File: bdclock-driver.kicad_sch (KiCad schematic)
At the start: 32 parts, among them J1 PWR, J2 Ctrl, J3 Anodes, J4 Kathodes, U1 NE555P, U2 74HC4017, U3 LM7805_TO220, U4 74HC595, U5 74HC595, U6 74HC595, U7 74LS138, U8 74LS138

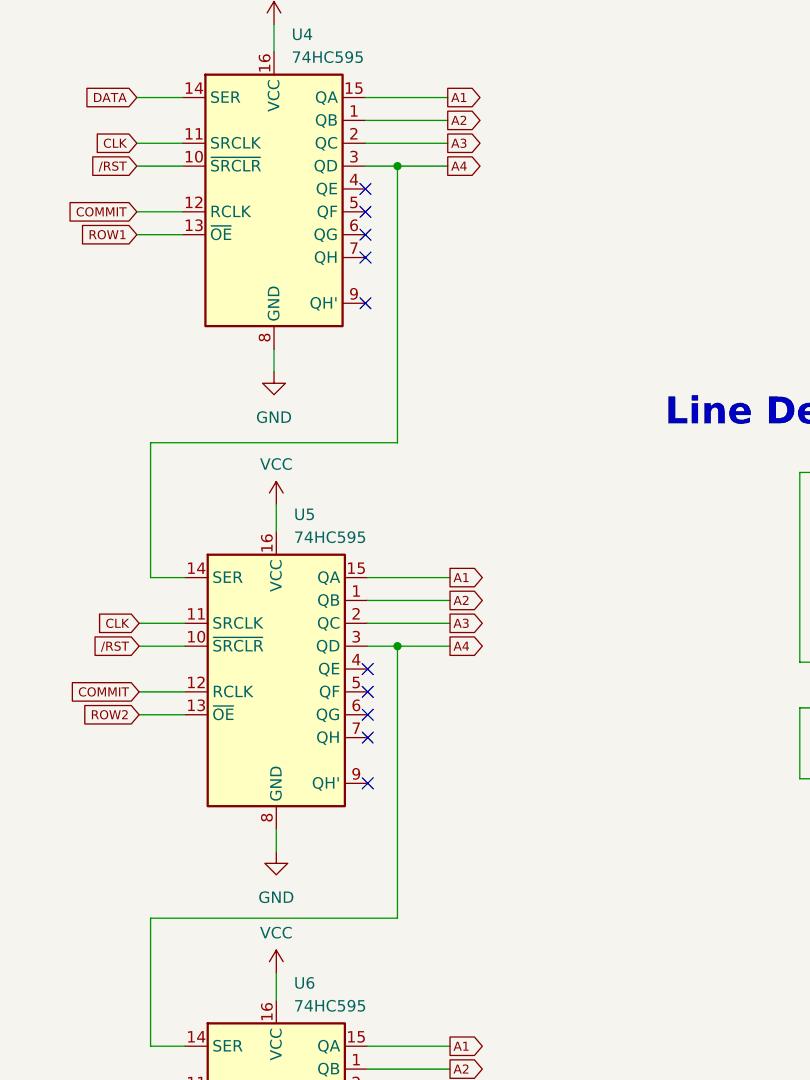
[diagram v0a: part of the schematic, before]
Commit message: :bug: Fix the wiring for the 595's cascading logic
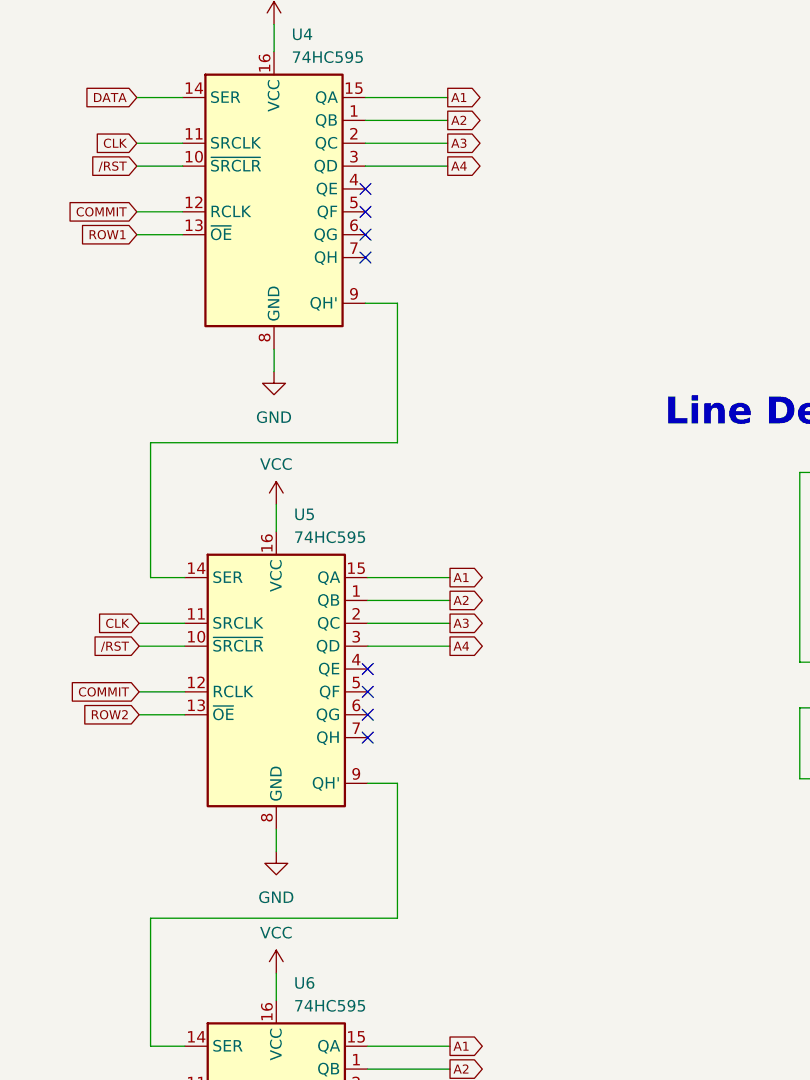
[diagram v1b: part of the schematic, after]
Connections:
- net A4: no longer U5.14 (SER), U6.14 (SER)
- net at U5.9 (QH'): now also U6.14 (SER)
- net at U4.9 (QH'): now also U5.14 (SER)
- no-connect marks 26 -> 24
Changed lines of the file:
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@@
   (junction (at 54.61 40.64) (diameter 0) (color 0 0 0 0)
   )
-  (junction (at 160.782 96.52) (diameter 0) (color 0 0 0 0)
-  )
   (junction (at 49.53 88.9) (diameter 0) (color 0 0 0 0)
   )
@@
   (junction (at 226.06 77.216) (diameter 0) (color 0 0 0 0)
   )
-  (junction (at 160.782 43.18) (diameter 0) (color 0 0 0 0)
-  )
   (junction (at 39.37 30.48) (diameter 0) (color 0 0 0 0)
   )
@@
   )
   (no_connect (at 76.2 165.1))
-  (no_connect (at 157.48 111.76))
   (no_connect (at 238.76 143.764))
   (no_connect (at 157.48 156.21))
@@
   (no_connect (at 238.76 148.844))
   (no_connect (at 238.76 146.304))
-  (no_connect (at 157.226 58.42))
   (no_connect (at 157.48 151.13))
   (no_connect (at 157.48 99.06))
@@
     (stroke (width 0) (type default))
   )
+  (wire (pts (xy 157.48 111.76) (xy 160.782 111.76))
+    (stroke (width 0) (type default))
+  )
   (wire (pts (xy 157.226 35.56) (xy 166.37 35.56))
     (stroke (width 0) (type default))
@@
     (stroke (width 0) (type default))
   )
-  (wire (pts (xy 157.226 43.18) (xy 160.782 43.18))
+  (wire (pts (xy 157.226 43.18) (xy 166.37 43.18))
     (stroke (width 0) (type default))
   )
@@
     (stroke (width 0) (type default))
   )
-  (wire (pts (xy 160.782 96.52) (xy 160.782 126.746))
-    (stroke (width 0) (type default))
-  )
   (wire (pts (xy 238.76 93.218) (xy 254 93.218))
     (stroke (width 0) (type default))
@@
     (stroke (width 0) (type default))
   )
+  (wire (pts (xy 160.782 111.76) (xy 160.782 126.746))
+    (stroke (width 0) (type default))
+  )
   (wire (pts (xy 157.48 93.98) (xy 166.624 93.98))
     (stroke (width 0) (type default))
@@
     (stroke (width 0) (type default))
   )
-  (wire (pts (xy 160.782 43.18) (xy 160.782 73.914))
-    (stroke (width 0) (type default))
-  )
-  (wire (pts (xy 160.782 43.18) (xy 166.37 43.18))
+  (wire (pts (xy 157.226 58.42) (xy 160.782 58.42))
     (stroke (width 0) (type default))
   )
@@
     (stroke (width 0) (type default))
   )
-  (wire (pts (xy 160.782 96.52) (xy 166.624 96.52))
-    (stroke (width 0) (type default))
-  )
   (wire (pts (xy 160.782 126.746) (xy 133.35 126.746))
     (stroke (width 0) (type default))
@@
     (stroke (width 0) (type default))
   )
-  (wire (pts (xy 157.48 96.52) (xy 160.782 96.52))
+  (wire (pts (xy 157.48 96.52) (xy 166.624 96.52))
     (stroke (width 0) (type default))
   )
@@
     (stroke (width 0) (type default))
   )
+  (wire (pts (xy 160.782 58.42) (xy 160.782 73.914))
+    (stroke (width 0) (type default))
+  )

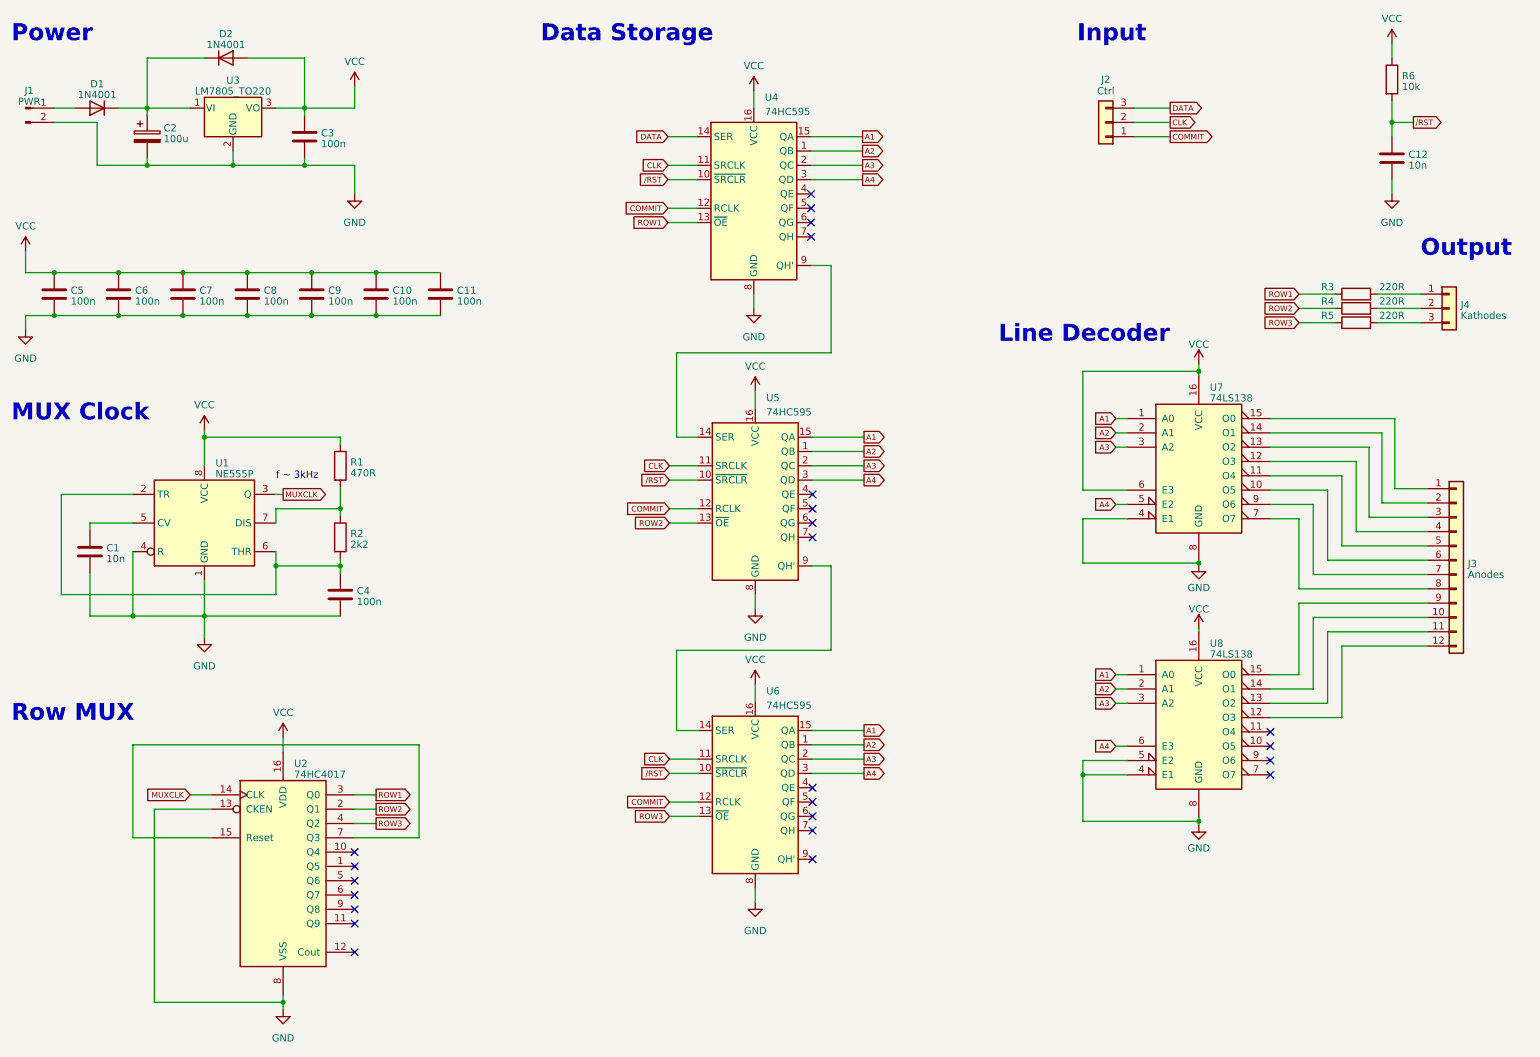
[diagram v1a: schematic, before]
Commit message: :wrench: Assign missing footprints
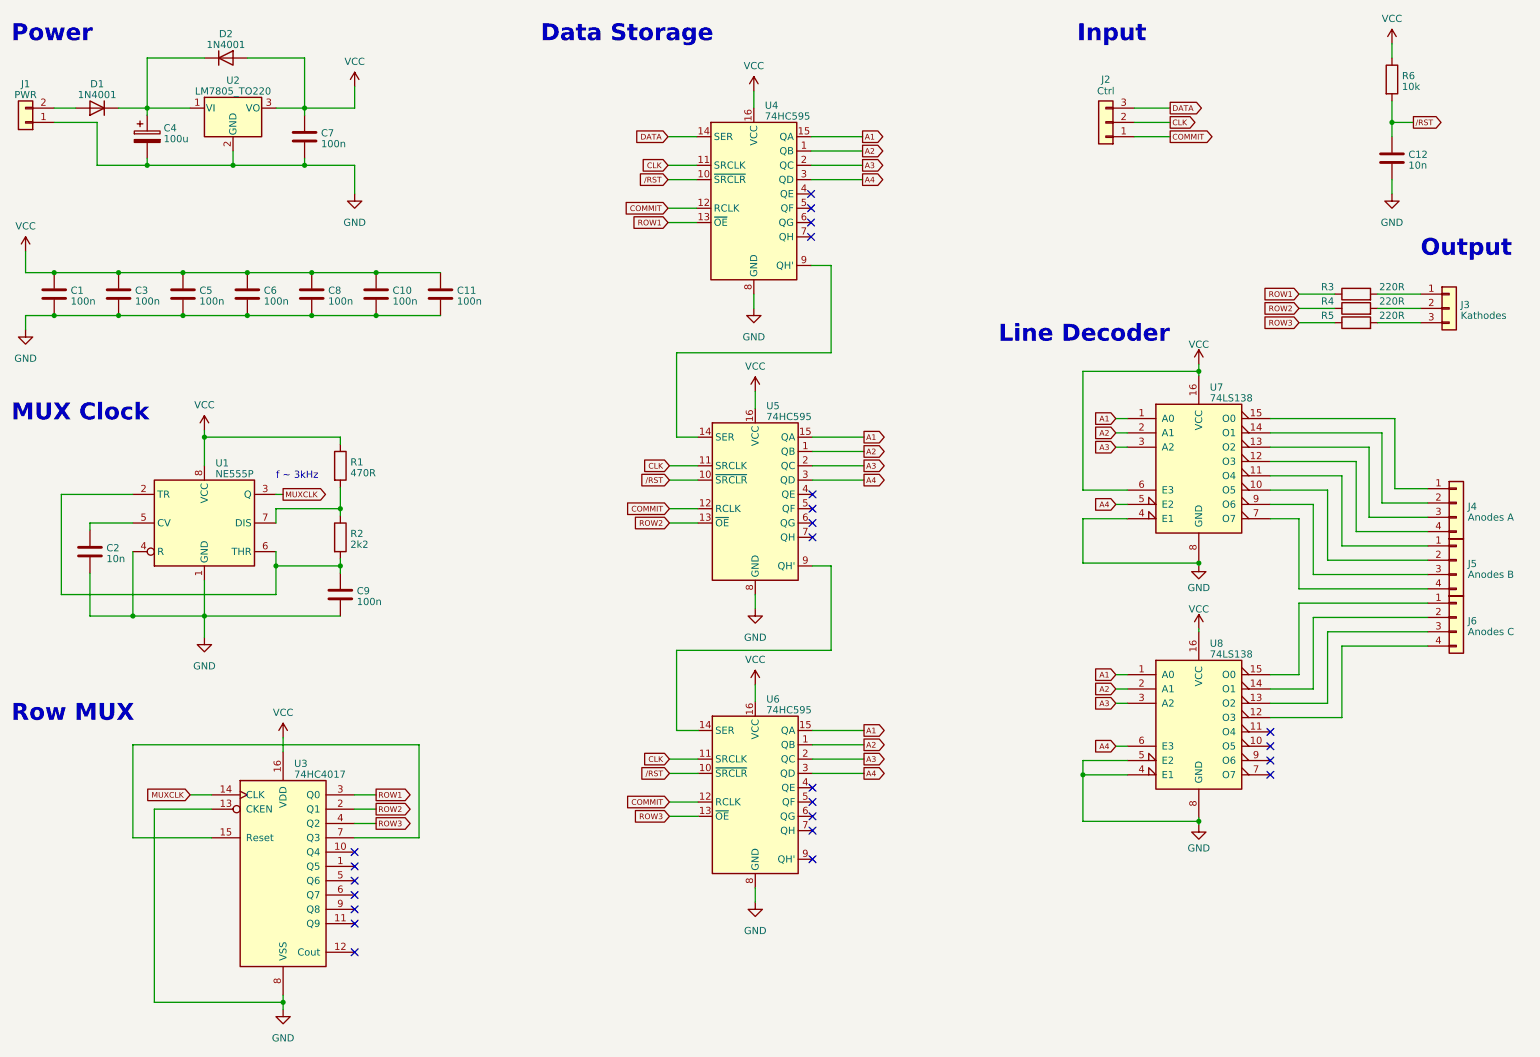
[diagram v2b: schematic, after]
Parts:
- added J5: Anodes B, TerminalBlock:TerminalBlock_Altech_AK300-4_P5.00mm, symbol Connector_Generic:Conn_01x04
- added J6: Anodes C, TerminalBlock:TerminalBlock_Altech_AK300-4_P5.00mm, symbol Connector_Generic:Conn_01x04
- C1: renamed from C5; footprint (none) -> Capacitor_THT:C_Disc_D4.3mm_W1.9mm_P5.00mm
- C10, C11, C12: footprint (none) -> Capacitor_THT:C_Disc_D4.3mm_W1.9mm_P5.00mm
- C2: renamed from C1; footprint (none) -> Capacitor_THT:C_Disc_D4.3mm_W1.9mm_P5.00mm
- C3: renamed from C6; footprint (none) -> Capacitor_THT:C_Disc_D4.3mm_W1.9mm_P5.00mm
- C4: renamed from C2; footprint (none) -> Capacitor_THT:CP_Radial_D6.3mm_P2.50mm; REICHELT (none) -> KA-A 100U 16
- C5: renamed from C7; footprint (none) -> Capacitor_THT:C_Disc_D4.3mm_W1.9mm_P5.00mm
- C6: renamed from C8; footprint (none) -> Capacitor_THT:C_Disc_D4.3mm_W1.9mm_P5.00mm
- C7: renamed from C3; footprint (none) -> Capacitor_THT:C_Disc_D4.3mm_W1.9mm_P5.00mm
- C8: renamed from C9; footprint (none) -> Capacitor_THT:C_Disc_D4.3mm_W1.9mm_P5.00mm
- C9: renamed from C4; footprint (none) -> Capacitor_THT:C_Disc_D4.3mm_W1.9mm_P5.00mm
- J1: footprint (none) -> TerminalBlock:TerminalBlock_Altech_AK300-2_P5.00mm; symbol Connector:Conn_01x02_Pin -> Connector_Generic:Conn_01x02
- J2: footprint (none) -> Connector_PinSocket_2.54mm:PinSocket_1x03_P2.54mm_Vertical
- J3: renamed from J4; footprint (none) -> TerminalBlock:TerminalBlock_Altech_AK300-3_P5.00mm
- J4: renamed from J3; value Anodes -> Anodes A; footprint (none) -> TerminalBlock:TerminalBlock_Altech_AK300-4_P5.00mm; symbol Connector_Generic:Conn_01x12 -> Connector_Generic:Conn_01x04
- R1, R2, R3, R4, R5, R6: footprint (none) -> Resistor_THT:R_Axial_DIN0207_L6.3mm_D2.5mm_P7.62mm_Horizontal
- U1: footprint Package_DIP:DIP-8_W7.62mm -> Package_DIP:DIP-8_W7.62mm_Socket_LongPads
- U3: renamed from U2; footprint (none) -> Package_DIP:DIP-16_W7.62mm_Socket_LongPads
- U4, U5, U6, U7, U8: footprint (none) -> Package_DIP:DIP-16_W7.62mm_Socket_LongPads
- renumbered U3 to U2
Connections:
- net GND: now also J1.1 (Pin_1); no longer J1.2 (Pin_2)
- net at U8.12 (O3): now also J6.4 (Pin_4); no longer J4.12 (Pin_12)
- net at U8.13 (O2): now also J6.3 (Pin_3); no longer J4.11 (Pin_11)
- net at U8.14 (O1): now also J6.2 (Pin_2); no longer J4.10 (Pin_10)
- net at U8.15 (O0): now also J6.1 (Pin_1); no longer J4.9 (Pin_9)
- net at D1.2 (A): now also J1.2 (Pin_2); no longer J1.1 (Pin_1)
- net at U7.10 (O5): now also J5.2 (Pin_2); no longer J4.6 (Pin_6)
- net at U7.11 (O4): now also J5.1 (Pin_1); no longer J4.5 (Pin_5)
- net at U7.7 (O7): now also J5.4 (Pin_4); no longer J4.8 (Pin_8)
- net at U7.9 (O6): now also J5.3 (Pin_3); no longer J4.7 (Pin_7)

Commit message: :art: Geographical renumeration of all components
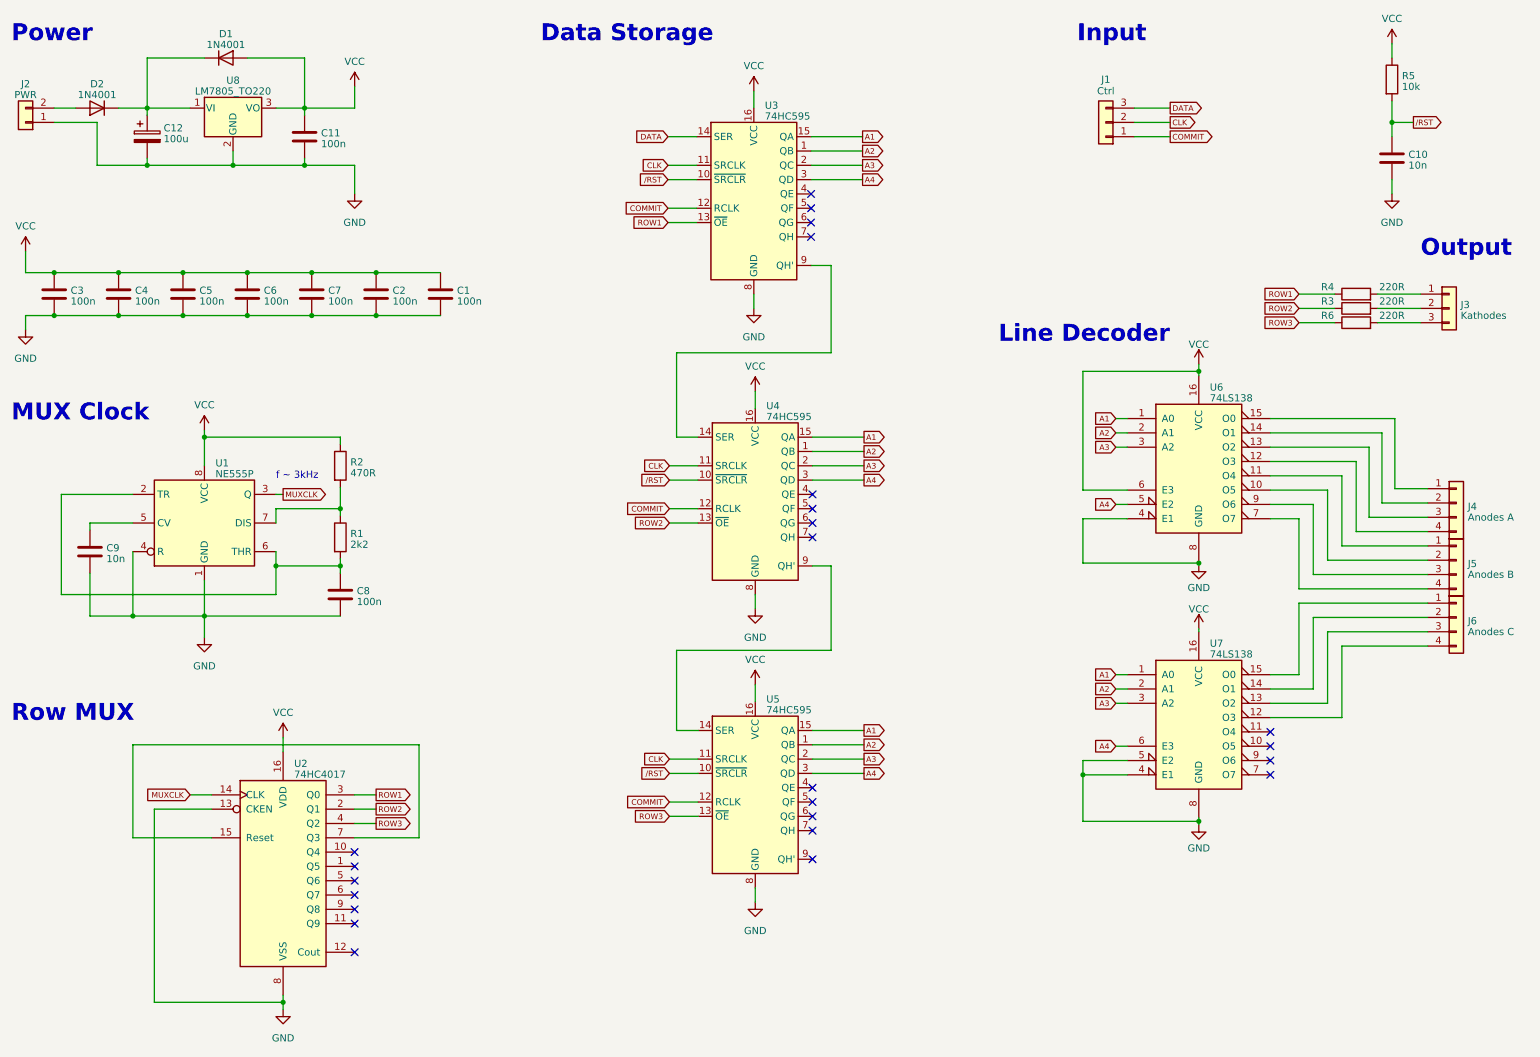
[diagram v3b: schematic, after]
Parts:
- renumbered C11 to C1, C12 to C10, C7 to C11, C4 to C12, C10 to C2, C1 to C3, C3 to C4, C8 to C7, C9 to C8, C2 to C9, D2 to D1, D1 to D2, J2 to J1, J1 to J2, R2 to R1, R1 to R2, R4 to R3, R3 to R4, R6 to R5, R5 to R6, U3 to U2, U4 to U3, U5 to U4, U6 to U5, U7 to U6, U8 to U7, U2 to U8

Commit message: :art: Place JLCPCB serial number marker and add GND to data connector
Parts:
- J1: footprint Connector_PinSocket_2.54mm:PinSocket_1x03_P2.54mm_Vertical -> Connector_PinSocket_2.54mm:PinSocket_1x04_P2.54mm_Vertical; symbol Connector_Generic:Conn_01x03 -> Connector_Generic:Conn_01x04
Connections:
- net GND: now also J1.4 (Pin_4)
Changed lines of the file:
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@@
+    (stroke (width 0) (type default))
+  )
+  (wire (pts (xy 214.63 27.94) (xy 233.045 27.94))
     (stroke (width 0) (type default))
   )
@@
   )
   (wire (pts (xy 226.06 77.216) (xy 226.06 77.978))
+    (stroke (width 0) (type default))
+  )
+  (wire (pts (xy 233.045 27.94) (xy 233.045 37.592))
     (stroke (width 0) (type default))
   )
@@
     )
   )
+  (symbol (lib_id "power:GND") (at 233.045 37.592 0) (unit 1)
+    (in_bom yes) (on_board yes) (dnp no) (fields_autoplaced)
+    (property "Reference" "#PWR021" (at 233.045 43.942 0)
+      (effects (font (size 1.27 1.27)) hide)
+    )
+    (property "Value" "GND" (at 233.045 42.672 0)
+      (effects (font (size 1.27 1.27)))
+    )
+    (property "Footprint" "" (at 233.045 37.592 0)
+      (effects (font (size 1.27 1.27)) hide)
+    )
+    (property "Datasheet" "" (at 233.045 37.592 0)
+      (effects (font (size 1.27 1.27)) hide)
+    )
+    (pin "1")
+    (instances
+      (project "bdclock-driver"
+        (path "/14a835c9-91cc-44a9-a6f5-f761c518c76f"
+          (reference "#PWR021") (unit 1)
+        )
+      )
+    )
+  )
   (symbol (lib_id "power:GND") (at 226.06 157.734 0) (unit 1)
     (in_bom yes) (on_board yes) (dnp no) (fields_autoplaced)
@@
     )
   )
-  (symbol (lib_id "Connector_Generic:Conn_01x03") (at 209.55 33.02 180) (unit 1)
+  (symbol (lib_id "Connector_Generic:Conn_01x04") (at 209.55 33.02 180) (unit 1)
     (in_bom yes) (on_board yes) (dnp no)
-    (property "Reference" "J1" (at 209.55 25.4 0)
+    (property "Reference" "J1" (at 209.55 23.622 0)
       (effects (font (size 1.27 1.27)))
     )
-    (property "Value" "Ctrl" (at 209.55 27.448 0)
+    (property "Value" "Ctrl" (at 209.55 25.527 0)
       (effects (font (size 1.27 1.27)))
     )
-    (property "Footprint" "Connector_PinSocket_2.54mm:PinSocket_1x03_P2.54mm_Vertical" (at 209.55 33.02 0)
+    (property "Footprint" "Connector_PinSocket_2.54mm:PinSocket_1x04_P2.54mm_Vertical" (at 209.55 33.02 0)
       (effects (font (size 1.27 1.27)) hide)
     )
@@
     (pin "2")
     (pin "3")
-    (instances
-      (project "bdclock-driver"
+    (pin "4")
+    (instances
+      (project "bdclock-driver"
